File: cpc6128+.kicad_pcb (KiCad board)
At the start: 2 copper layers, 284 x 140.5 mm, 199 parts, among them IC101 AMS40489, IC102 z80_6128, IC103 SED9420Cac, IC104 UPD765AC-2, IC105 74LS38, IC106 74LS38, IC107 74HC14, IC108 MC74HC4051N, IC109 LA6393D, IC110 41464, IC111 41464, IC112 41464, IC113 41464, IC114 AY38912, IC115 AMS40464, IC116 74HCT02, J101 rj12, J102 audio/video, J103 Jack audio, J104 POWER_JACK_6128, Q101 KTC1815Y, Q103 KTC1815Y, Q104 KTC1815Y, Q105 KTC1815Y, Q106 KTC1815Y, Q107 KTC1815Y, SW1 SW_DIP_x01, X181 40 MHz

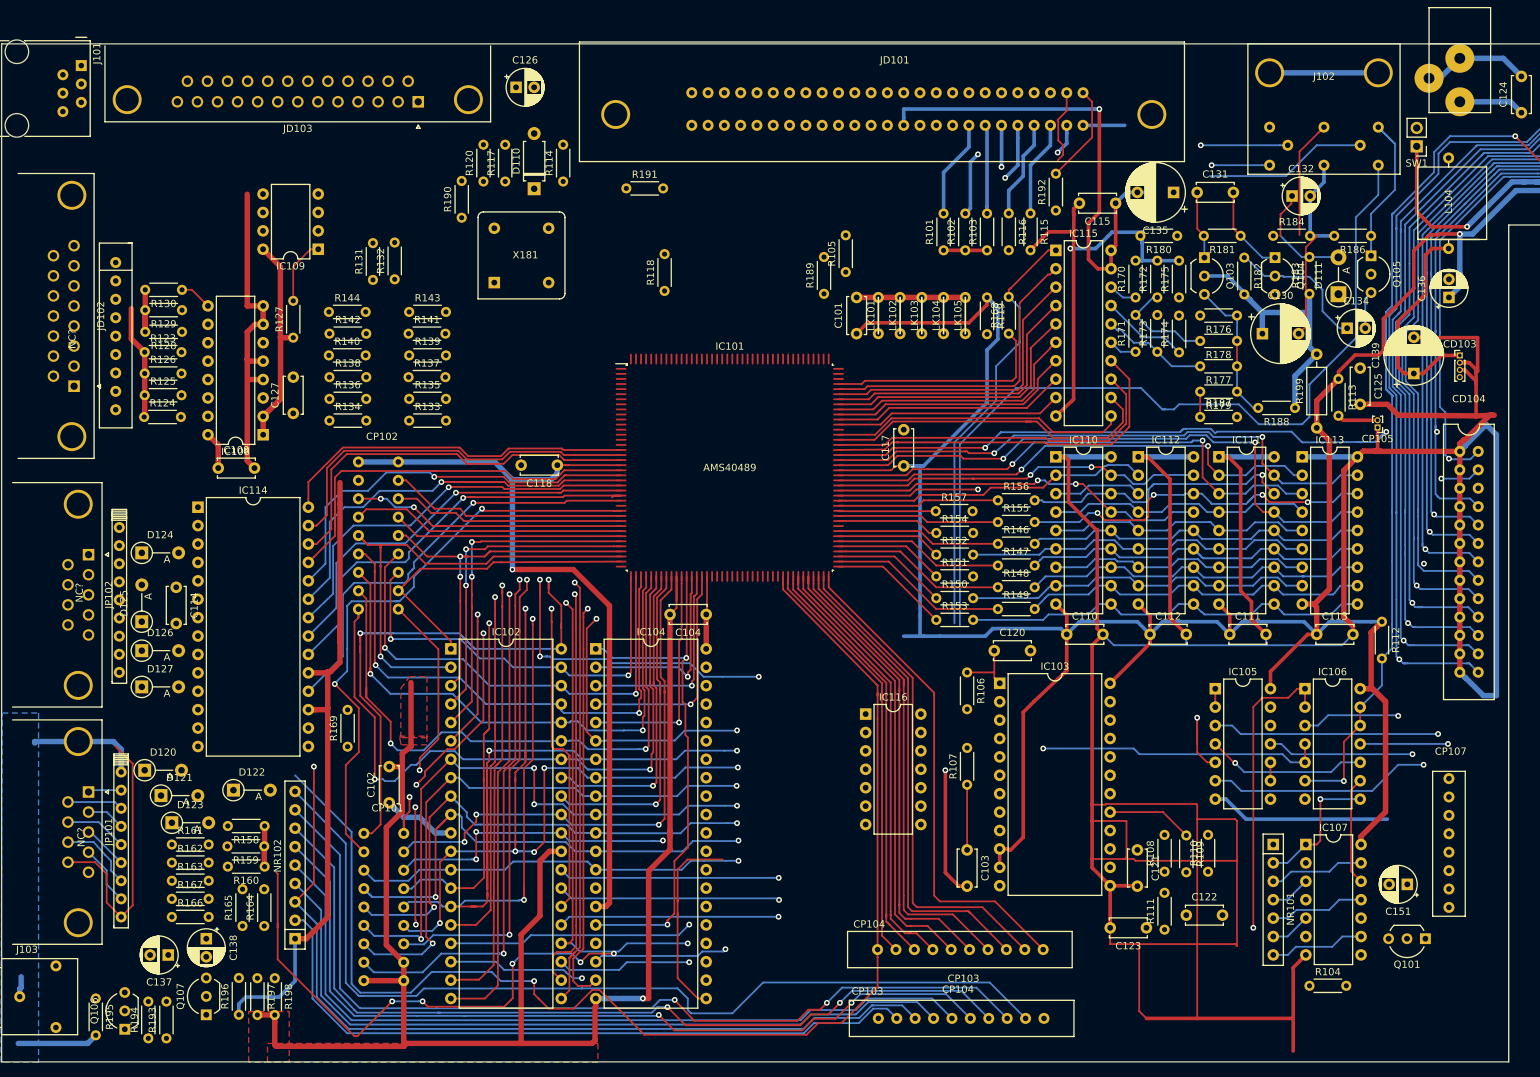
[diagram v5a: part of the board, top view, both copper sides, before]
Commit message: More work on the db25 part, & the 50 way centronic connector
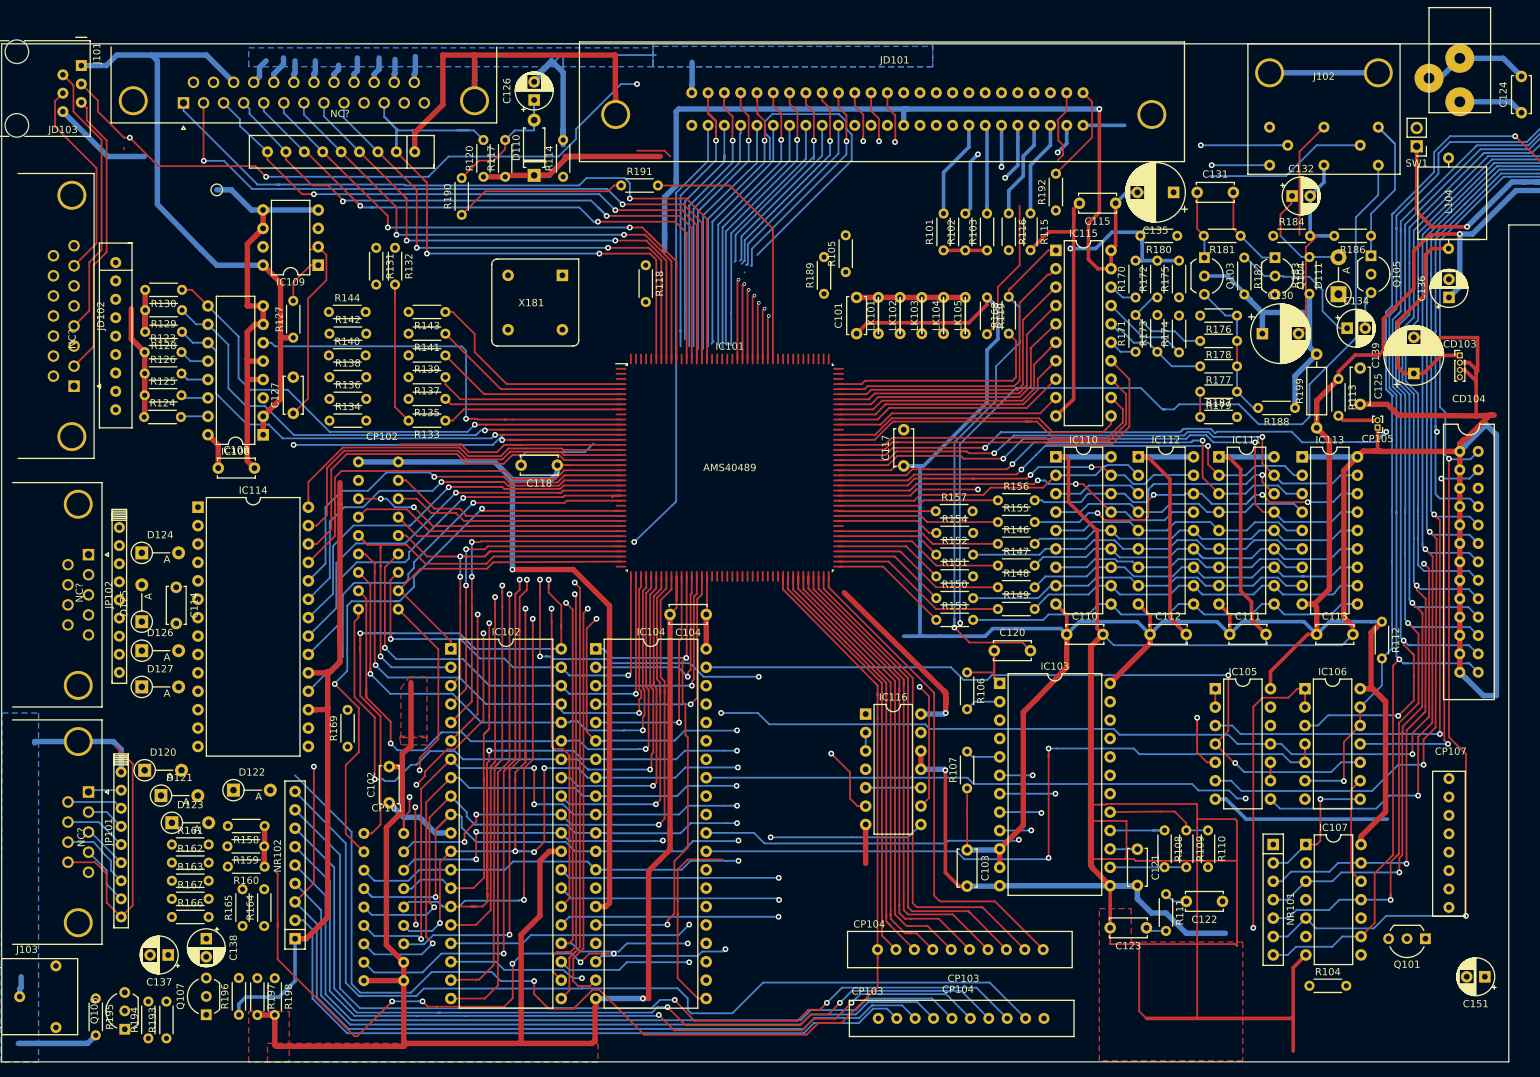
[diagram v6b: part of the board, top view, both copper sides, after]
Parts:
- added NC?: nc_db25_db15, cpc6128+:nc_db25_db15, F.Cu at (70.7, 35.4)
- JD103: footprint Connector_Dsub:DSUB-25_Male_Horizontal_P2.77x2.84mm_EdgePinOffset4.94mm_Housed_MountingHolesOffset7.48mm -> Connector_Dsub:DSUB-25_Female_Horizontal_P2.77x2.84mm_EdgePinOffset4.94mm_Housed_MountingHolesOffset7.48mm
- moved JD103 32.4 mm to (49.1, 30.4)
- moved X181 30.2 mm to (100.9, 69.2), turned to 180 degrees
- moved C151 16.6 mm to (228.7, 151.0)
- moved R108 5.70 mm to (184.5, 130.8), turned to 270 degrees
- moved R110 5.70 mm to (190.5, 130.8), turned to 270 degrees
- moved C122 5.35 mm to (192.5, 140.6), turned to 180 degrees
- moved R137 5.08 mm to (85.2, 68.2), turned to 180 degrees
- moved R141 5.08 mm to (85.2, 62.2), turned to 180 degrees
- moved R133 5.00 mm to (85.2, 74.2), turned to 180 degrees
- moved R135 5.00 mm to (85.2, 71.2), turned to 180 degrees
- moved R139 5.00 mm to (85.2, 65.2), turned to 180 degrees
- moved R143 5.00 mm to (85.2, 59.2), turned to 180 degrees
- moved R111 4.90 mm to (184.7, 139.6), turned to 270 degrees
- moved R131 4.45 mm to (75.7, 50.4), turned to 270 degrees
- moved R118 4.40 mm to (112.9, 52.8), turned to 270 degrees
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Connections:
- IC103 pad 15: (no net) -> Net-(C121-Pad1)
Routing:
- net GND: track 992.7 -> 1196.2 mm
- net +5V: track 759.5 -> 932.8 mm
- net Net-(IC104-Pad30): track 24.7 -> 151.9 mm, vias 1 -> 3
- net /FloppyDisk/~WGATE: track 146.2 -> 251.5 mm, vias 2 -> 3
- net /gateArray/PSTB: track 0.00 -> 101.3 mm, vias 0 -> 1
- net /gateArray/PR0: track 0.00 -> 99.7 mm, vias 0 -> 2
- net (no net): track 214.8 -> 311.2 mm, vias 12 -> 13
- net /gateArray/PR1: track 0.00 -> 92.3 mm, vias 0 -> 2
- net /gateArray/PR2: track 0.00 -> 90.1 mm, vias 0 -> 2
- net /gateArray/BUSY: track 0.00 -> 90.0 mm, vias 0 -> 2
- net LPEN: track 4.27 -> 93.3 mm, vias 1 -> 4
- net /FloppyDisk/~INDEX: track 87.0 -> 174.5 mm, vias 2 -> 3
- net /gateArray/PR3: track 0.00 -> 86.5 mm, vias 0 -> 2
- net /gateArray/PR4: track 0.00 -> 79.5 mm, vias 0 -> 2
- net /gateArray/PR5: track 0.00 -> 76.7 mm, vias 0 -> 2
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
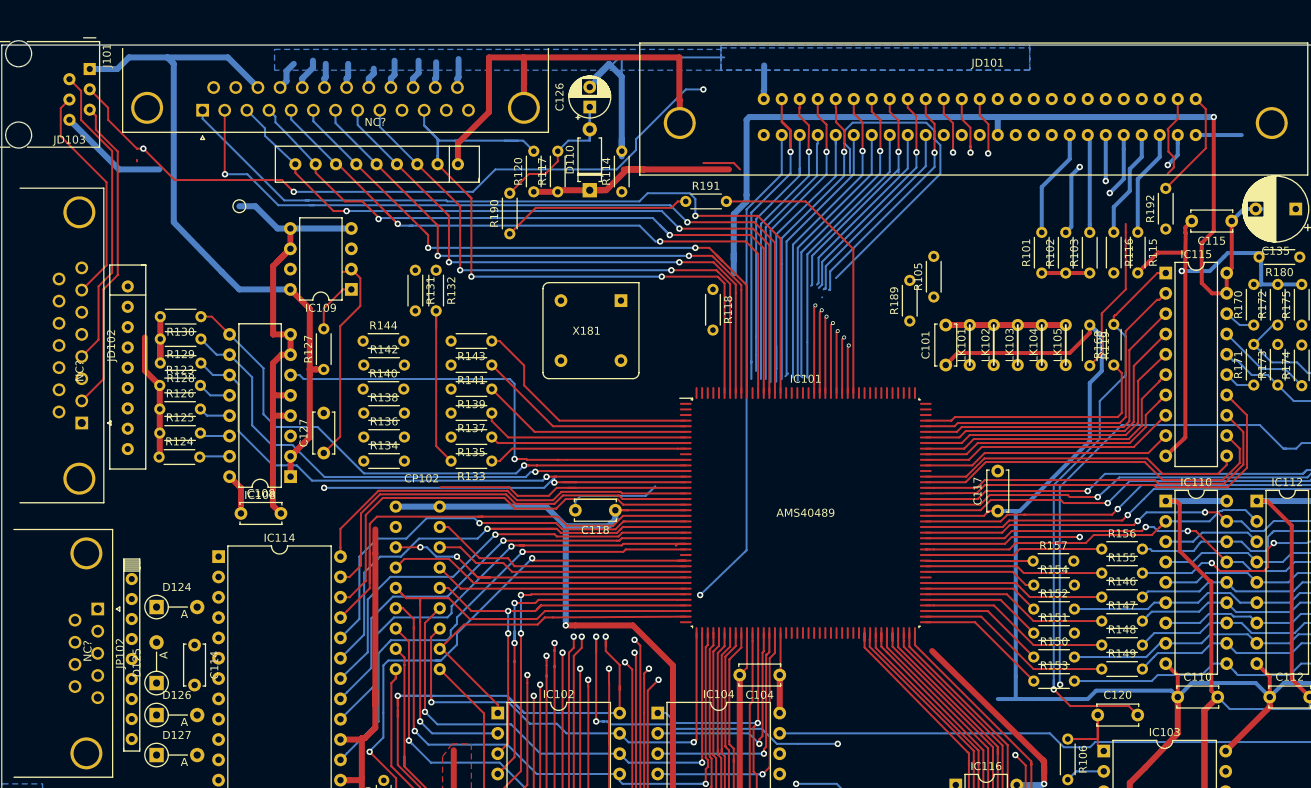
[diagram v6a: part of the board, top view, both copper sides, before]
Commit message: More work on centronics port.
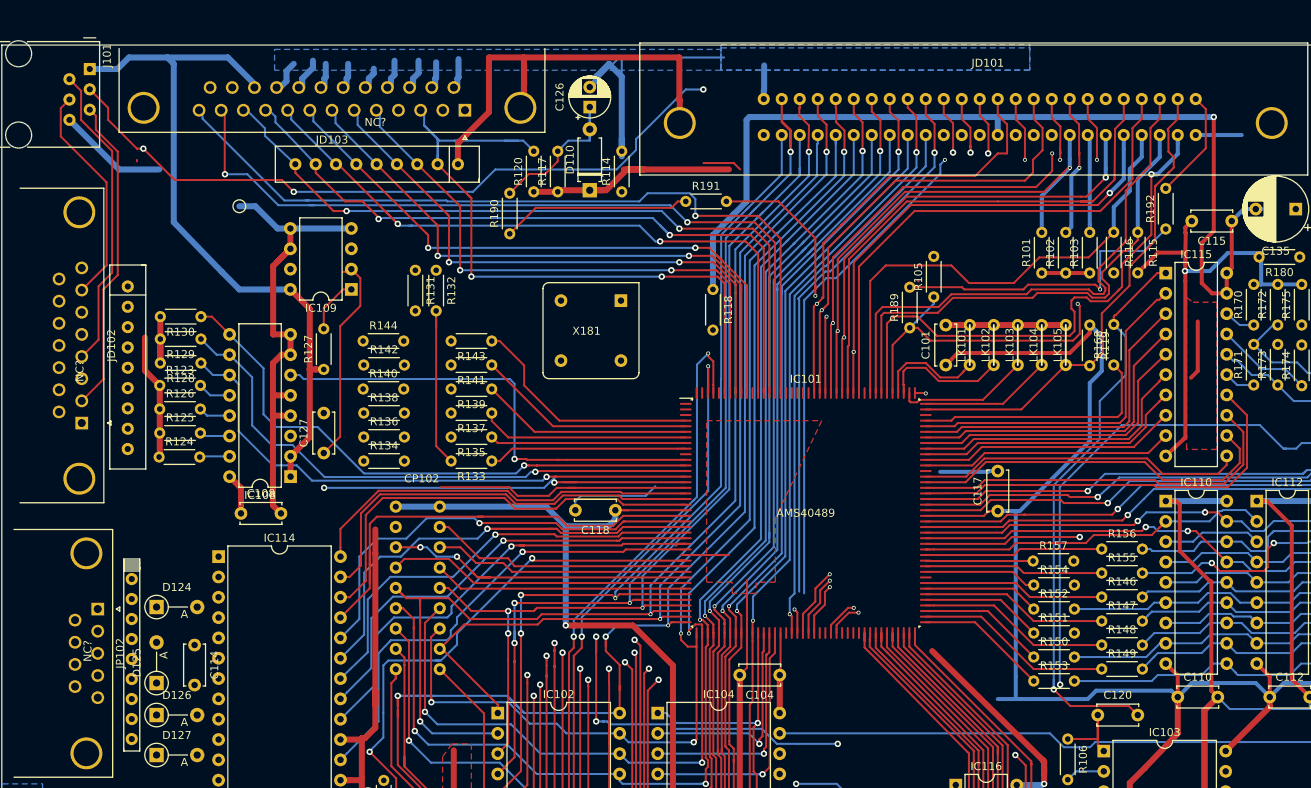
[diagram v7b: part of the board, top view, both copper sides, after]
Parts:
- JD103: footprint Connector_Dsub:DSUB-25_Female_Horizontal_P2.77x2.84mm_EdgePinOffset4.94mm_Housed_MountingHolesOffset7.48mm -> Connector_Dsub:DSUB-25_Male_Horizontal_P2.77x2.84mm_EdgePinOffset4.94mm_Housed_MountingHolesOffset7.48mm
- moved JD103 32.8 mm to (81.9, 30.4)
- moved R189 0.85 mm to (137.5, 57.6)
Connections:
- net /CPU/~BUSAK renamed ~BUSACK
- net /CPU/~BUSRQ renamed ~BUSRQ
- net /CPU/~HALT renamed ~HALT
- net /CPU/~NMI renamed ~NMI
- net /CPU/~RFSH renamed ~RFSH
- IC101 pad 133: NROMEN -> ~ROMEN
- IC101 pad 135: /gateArray/~INT -> ~INT
- IC101 pad 136: /gateArray/~WR -> ~WR
- IC101 pad 138: /gateArray/~RD -> ~RD
- IC101 pad 139: /gateArray/~MREQ -> ~MREQ
- IC101 pad 66: /gateArray/~M1 -> ~M1
- IC102 pad 16: /CPU/~INT -> ~INT
- IC102 pad 19: /CPU/~MREQ -> ~MREQ
- IC102 pad 21: /CPU/~RD -> ~RD
- IC102 pad 22: /CPU/~WR -> ~WR
- IC102 pad 27: /CPU/~MI -> ~M1
- JD101 pad 28: /CPU/~MREQ -> ~MREQ
- JD101 pad 29: /CPU/~M1 -> ~M1
- JD101 pad 32: /CPU/~RD -> ~RD
- JD101 pad 33: /CPU/~RW -> ~WR
- JD101 pad 35: /CPU/~INT -> ~INT
- LK101 pad 1: (no net) -> /gateArray/LK101
- LK102 pad 1: (no net) -> /gateArray/LK102
- LK103 pad 1: (no net) -> /gateArray/LK103
- LK104 pad 1: (no net) -> /gateArray/LK104
- LK105 pad 1: Net-(IC101-Pad119) -> /gateArray/LK105
- R101 pad 2: /CPU/~INT -> ~INT
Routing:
- net ~RD: track 0.00 -> 118.6 mm, vias 0 -> 2
- net ~MREQ: track 0.00 -> 114.9 mm, vias 0 -> 2
- net ~INT: track 0.00 -> 114.2 mm, vias 0 -> 3
- net ~WR: track 0.00 -> 108.0 mm, vias 0 -> 3
- net CLK4: track 88.7 -> 167.8 mm, vias 2 -> 4
- net CURSOR: track 0.00 -> 68.1 mm
- net ~ROMEN: track 0.00 -> 65.6 mm
- net LPEN: track 93.3 -> 158.8 mm
- net ~RAMRD: track 0.00 -> 65.0 mm
- net /CPU/~INT: track 63.6 -> 0.00 mm, vias 1 -> 0
- net /CPU/~MREQ: track 60.6 -> 0.00 mm, vias 1 -> 0
- net /CPU/~RD: track 59.8 -> 0.00 mm, vias 1 -> 0
- net /CPU/~WR: track 56.8 -> 0.00 mm, vias 1 -> 0
- net RAMDIS: track 13.3 -> 63.2 mm
- net ROMDIS: track 13.6 -> 63.0 mm
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
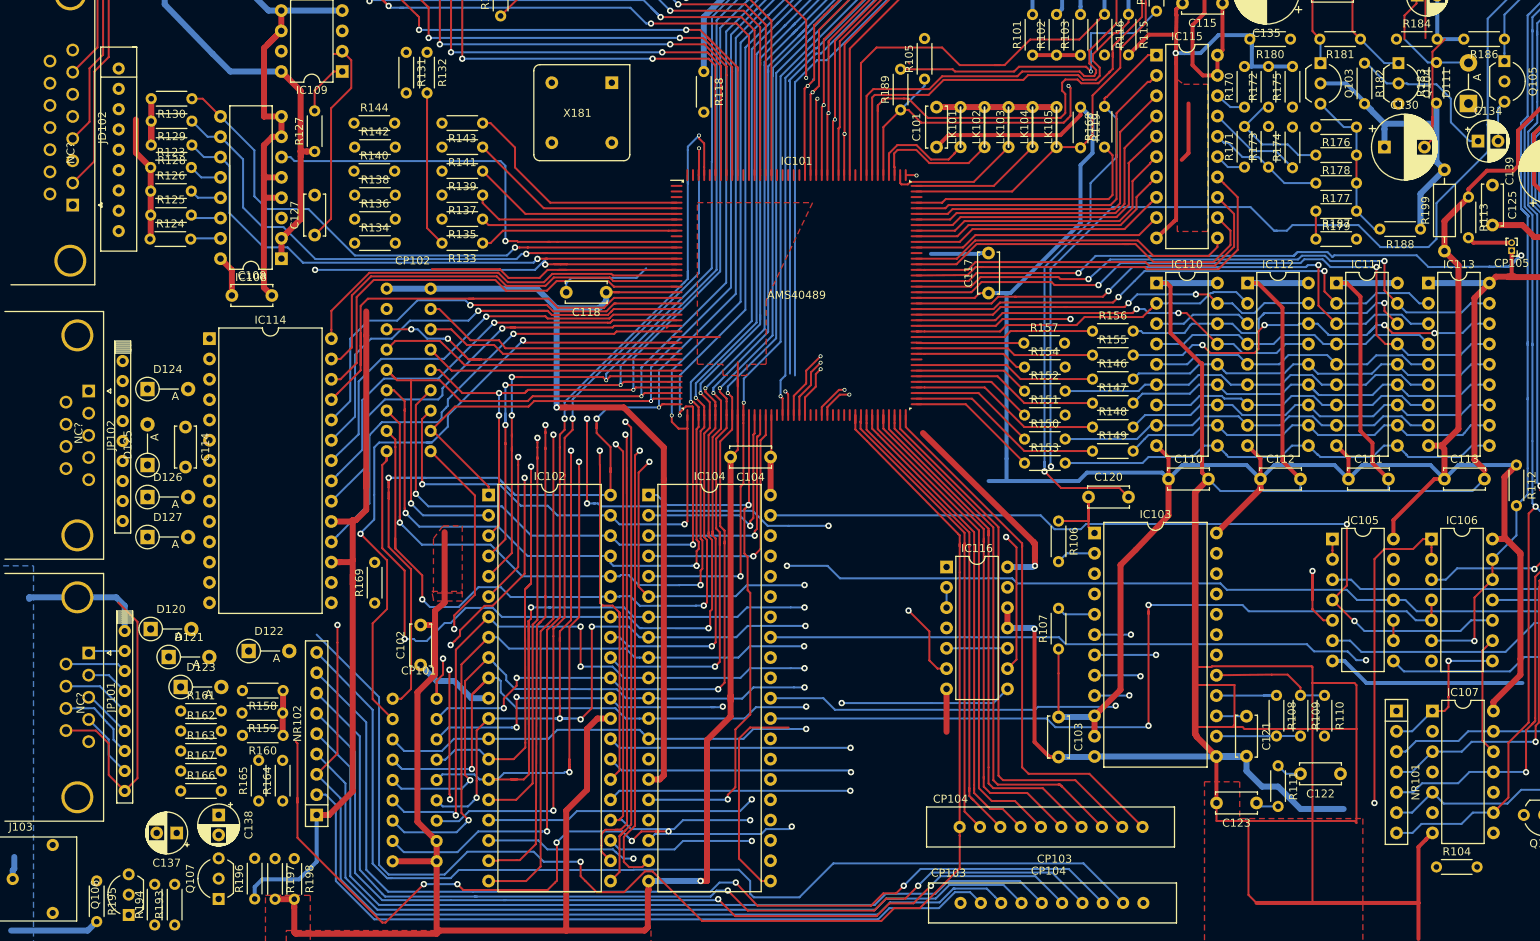
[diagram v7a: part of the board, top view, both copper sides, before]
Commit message: work around IC14
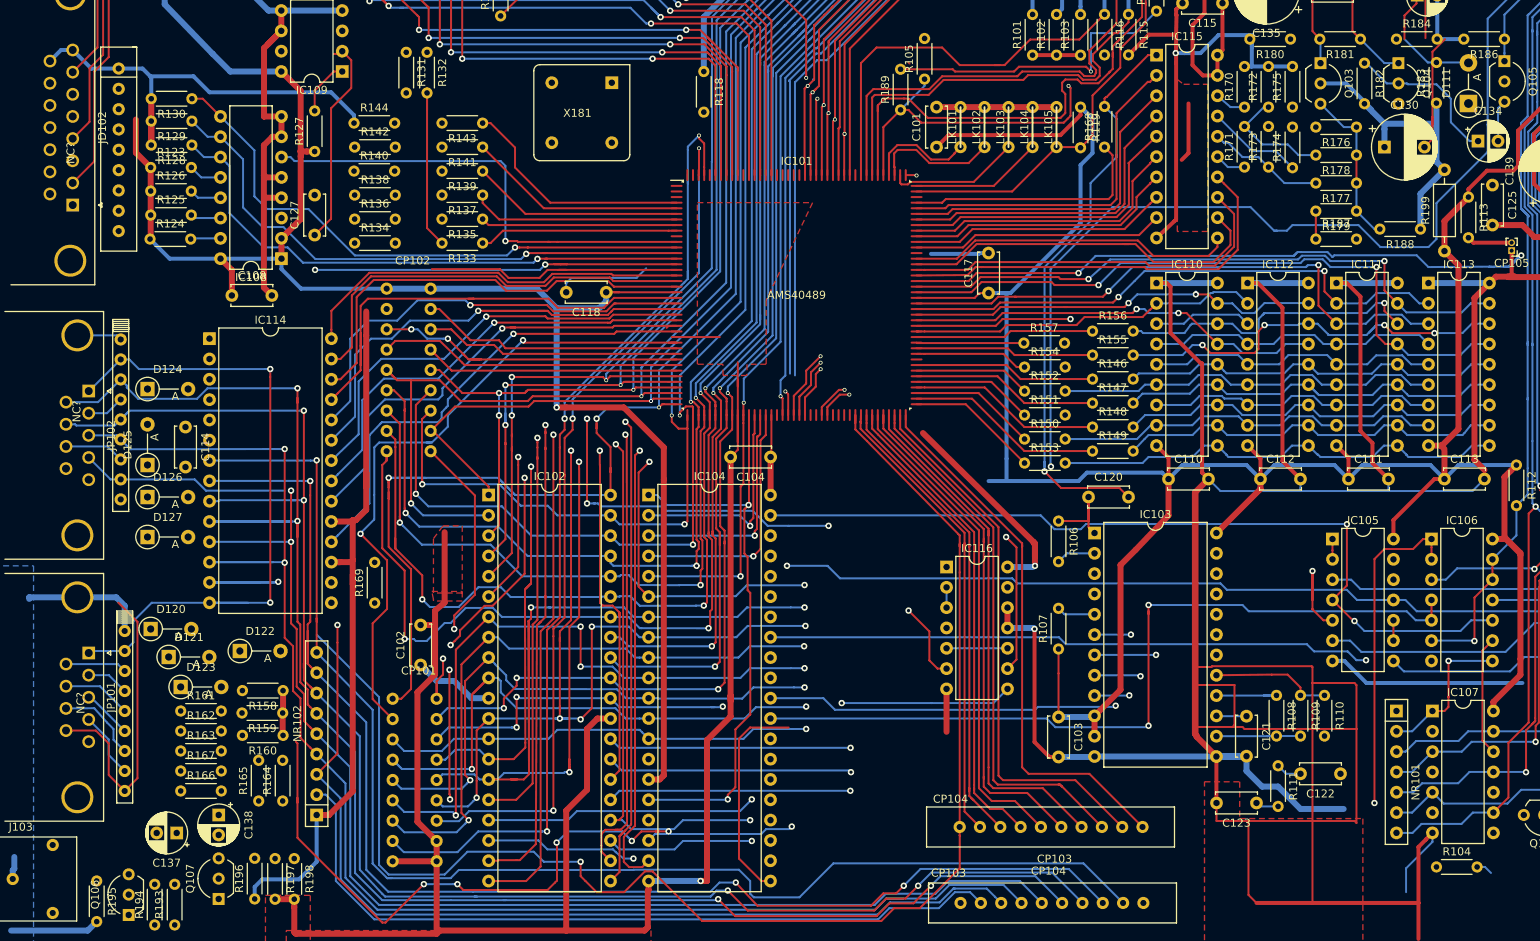
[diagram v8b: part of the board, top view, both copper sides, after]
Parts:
- moved NC? 2.71 mm to (36.5, 95.8)
- moved D122 1.10 mm to (54.9, 125.2)
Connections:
- IC107 pad 14: (no net) -> +5V
- IC107 pad 7: (no net) -> GND
- JP102 pad 1: Net-(JP102-Pad1) -> X8
- JP102 pad 3: Net-(JP102-Pad3) -> X6
- JP102 pad 4: Net-(JP102-Pad4) -> X5
- JP102 pad 6: Net-(JP102-Pad6) -> X4
- JP102 pad 7: Net-(JP102-Pad7) -> X3
- NC? pad 2: (no net) -> X5
- NC? pad 3: (no net) -> Net-(JP102-Pad8)
- NC? pad 4: (no net) -> X6
- NC? pad 5: (no net) -> X3
- NC? pad 6: (no net) -> Net-(JP102-Pad2)
- NC? pad 7: (no net) -> X4
- NC? pad 8: (no net) -> X8
- NC? pad 8: Net-(JP101-Pad1) -> X8
- NC? pad 9: (no net) -> GND
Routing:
- net X4: track 116.4 -> 213.6 mm, vias 2 -> 4
- net X6: track 105.3 -> 187.7 mm, vias 0 -> 2
- net X3: track 121.3 -> 202.6 mm, vias 2 -> 4
- net X8: track 97.0 -> 177.9 mm, vias 0 -> 2
- net X5: track 109.9 -> 178.0 mm, vias 0 -> 2
- net GND: track 1207.5 -> 1262.1 mm
- net X2: track 125.8 -> 167.1 mm, vias 2 -> 3
- net X1: track 131.1 -> 168.5 mm, vias 0 -> 1
- net +5V: track 914.3 -> 947.2 mm
- net X7: track 120.8 -> 143.9 mm, vias 1 -> 2
- net Net-(JP102-Pad8): track 0.00 -> 7.51 mm
- net (no net): track 318.6 -> 324.3 mm
- net Net-(JP102-Pad2): track 0.00 -> 4.71 mm
- net PC4: track 0.00 -> 2.05 mm
- net Net-(IC101-Pad15): track 54.9 -> 54.1 mm
